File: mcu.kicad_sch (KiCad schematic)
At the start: 17 parts, among them J2 U.FL-R-SMT-1(10), U1 SF32LB525UC6, U6 GD25Q64ESIG, Y1 32.768khz, Y2 48MHz

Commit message: save progress before refactor
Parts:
- removed U6: GD25Q64ESIG, GD25Q64ESIG:SOP-8_L5.3-W5.3-P1.27-LS8.0-BL, symbol GD25Q64ESIG:GD25Q64ESIG
- removed Y1: 32.768khz, Crystal:Crystal_SMD_2520-4Pin_2.5x2.0mm, symbol Device:Crystal_Small
- added TP8: SCL, TestPoint:TestPoint_Pad_1.5x1.5mm, symbol Connector:TestPoint
- added TP9: SDA, TestPoint:TestPoint_Pad_1.5x1.5mm, symbol Connector:TestPoint
- added U6: GD25Q64CWIGR, GD25Q64CWIGR:WSON-8_L6.0-W5.0-P1.27-BL-EP, symbol GD25Q64CWIGR:GD25Q64CWIGR
- added Y3: 32.768khz, symbol Device:Crystal_Small
- AE1: LCSC Part (none) -> C89334
- C20, C22, C23, L2, L3: now not fitted; now left out of the parts list
- C21: LCSC Part (none) -> C1548
- C24: LCSC Part (none) -> C1525
- J2: LCSC Part (none) -> C88374; now not fitted
- R10, R9: LCSC Part (none) -> C25744
- TP1, TP2: now left out of the parts list
- U1: LCSC Part (none) -> C47355842
- Y2: LCSC Part (none) -> C2932991
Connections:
- net +3V3: now also U6.8 (VCC)
- net FLASH_CLK: now also U6.6 (SCLK)
- net FLASH_CS: now also U6.1 (~{CS})
- net FLASH_DIO0: now also U6.5 (SI(IO0))
- net FLASH_DIO1: now also U6.2 (SO(IO1))
- net FLASH_DIO2: now also U6.3 (WP#(IO2))
- net FLASH_DIO3: now also U6.7 (HOLD#(IO3))
- net GND: now also U6.4 (VSS), U6.9 (EP)
- net SCL: now also TP8.1
- net SDA: now also TP9.1
- net at U1.11 (PA22): now also Y3.2
- net at U1.10 (PA23): now also Y3.1
- net HAPTIC_PWM: now reaches U1.25 (PA20)
- net OLED_EN: now reaches U1.49 (PA2)
- net LED_CLK: now reaches U1.5 (PA28)
- net LED_EN: now reaches U1.6 (PA27)
- net LED_DAT: now reaches U1.9 (PA24)
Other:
- moved on the sheet: C24

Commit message: progress dump
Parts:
- added R45, R46: 4.7k, Resistor_SMD:R_0402_1005Metric, symbol Device:R_Small
- added TP10: SCL, symbol Connector:TestPoint
- added TP11: TestPoint, symbol Connector:TestPoint
- R10, R9: value 10k -> 4.7k
- TP8: value SCL -> SCL_G1
- TP9: value SDA -> SDA_G1
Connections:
- net +3V3: now also R45.2, R46.2; no longer R10.2, R9.2
- net SCL: now also R46.1, TP10.1; no longer R10.1, TP8.1
- net SDA: now also R45.1, TP11.1; no longer R9.1, TP9.1
- net SDA_G1: now reaches U1.1 (PA32)
- net SDA_G1: now also R9.1, TP9.1
- net TOUCH_RST: now reaches U1.56 (PA44)
- net TOUCH_INT: now reaches U1.57 (PA43)
- net SCL_G1: now reaches U1.67 (PA33)
- net SCL_G1: now also R10.1, TP8.1
- net LED_CLK: no longer names the net of U1.5 (PA28)
- new net +3V3_G1: R10.2, R9.2
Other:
- moved on the sheet: C24, R10, R9, TP8, TP9, U6

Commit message: finish up everything but nfc
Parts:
- removed U6: GD25Q64CWIGR, GD25Q64CWIGR:WSON-8_L6.0-W5.0-P1.27-BL-EP, symbol GD25Q64CWIGR:GD25Q64CWIGR
- added R47: 100k, Resistor_SMD:R_0402_1005Metric, symbol Device:R_Small
- added R48: 47k, Resistor_SMD:R_0402_1005Metric, symbol Device:R_Small
- added R49: 7.5k, Resistor_SMD:R_0603_1608Metric, symbol Device:R_Small
- added TP12: UART2_TX, TestPoint:TestPoint_Pad_D1.0mm, symbol Connector:TestPoint
- added TP13: UART2_RX, TestPoint:TestPoint_Pad_D1.0mm, symbol Connector:TestPoint
- added U12: MKDV1GCL-ABA, MKDV1GCL-ABA:LGA-8_L6.0-W8.0-P1.27-TL, symbol MKDV1GCL-ABA:MKDV1GCL-ABA
- R10, R45, R46, R9: LCSC Part C25744 -> C25900
- TP10: footprint (none) -> TestPoint:TestPoint_Pad_D1.0mm; now left out of the parts list
- TP11: value TestPoint -> SDA; footprint (none) -> TestPoint:TestPoint_Pad_D1.0mm; now left out of the parts list
- TP8: value SCL_G1 -> SCL_G2; footprint TestPoint:TestPoint_Pad_1.5x1.5mm -> TestPoint:TestPoint_Pad_D1.0mm
- TP9: value SDA_G1 -> SDA_G2; footprint TestPoint:TestPoint_Pad_1.5x1.5mm -> TestPoint:TestPoint_Pad_D1.0mm
- Y3: footprint (none) -> Crystal:Crystal_SMD_2012-2Pin_2.0x1.2mm; LCSC Part (none) -> C99009
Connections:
- net +3V3: no longer C24.1
- net +3V3_G1: now also C24.1, R49.1, U12.8 (VDD); no longer R10.2, R9.2
- net GND: now also U12.4 (GND)
- net HAPTIC_PWM: now also U1.6 (PA27); no longer U1.25 (PA20)
- net LED_DAT: now also U1.63 (PA37); no longer U1.9 (PA24)
- net LED_EN: now also U1.62 (PA38); no longer U1.6 (PA27)
- net TOUCH_INT: now also R47.1
- net TOUCH_RST: now also R48.1
- net UART2_RX: now reaches U1.35 (PA10)
- net UART2_RX: now also TP13.1
- net UART2_TX: now reaches U1.42 (PA9)
- net UART2_TX: now also TP12.1
- net ACC_INT: now reaches U1.61 (PA39)
- net RF_WAKE: now reaches U1.8 (PA25)
- net FLASH_CLK renamed SD_DAT0
- net SD_DAT0: now also U12.6 (DAT0)
- net FLASH_CS renamed SD_DAT2
- net SD_DAT2: now also U12.1 (DAT2)
- net FLASH_DIO0 renamed SD_CMD
- net SD_CMD: now also U12.5 (CMD)
- net FLASH_DIO1 renamed SD_DAT3
- net SD_DAT3: now also R49.2, U12.2 (DAT3)
- net FLASH_DIO2 renamed SD_CLK
- net SD_CLK: now also U12.3 (CLK)
- net FLASH_DIO3 renamed SD_DAT1
- net SD_DAT1: now also U12.7 (DAT1)
- net SCL_G1 renamed SCL_G2
- net SDA_G1 renamed SDA_G2
- new net +3V3_G2: R10.2, R47.2, R48.2, R9.2
- new net FUEL_GPOUT: U1.25 (PA20)
- new net RF_DAT: U1.9 (PA24)
- no-connect marks 5 -> 15
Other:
- note added: "Pull up to configure boot from SD Card"
- moved on the sheet: C24, R45, R46, TP10, TP11

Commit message: progress
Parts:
- removed R10, R9: 4.7k, Resistor_SMD:R_0402_1005Metric, symbol Device:R_Small
- removed R48: 47k, Resistor_SMD:R_0402_1005Metric, symbol Device:R_Small
- R45, R46: footprint Resistor_SMD:R_0402_1005Metric -> (none); LCSC Part C25900 -> (none)
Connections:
- net +3V3: now also R45.1, R46.1; no longer R45.2, R46.2
- net ACC_INT: now also U1.57 (PA43); no longer U1.61 (PA39)
- net HAPTIC_PWM: now also U1.4 (PA29); no longer U1.6 (PA27)
- net LED_DAT: now also U1.9 (PA24); no longer U1.63 (PA37)
- net LED_EN: now also U1.5 (PA28); no longer U1.62 (PA38)
- net RF_DAT: now also U1.8 (PA25); no longer U1.9 (PA24)
- net RF_WAKE: now also U1.7 (PA26); no longer U1.8 (PA25)
- net SCL: now also R46.2, U1.58 (PA42); no longer R46.1, U1.59 (PA41)
- net SCL_G2: no longer U1.67 (PA33)
- net SDA: now also R45.2, U1.59 (PA41); no longer R45.1, U1.60 (PA40)
- net SDA_G2: no longer U1.1 (PA32)
- net TOUCH_INT: now also U1.6 (PA27); no longer U1.57 (PA43)
- net SCL_T2: now reaches U1.2 (PA31)
- net SDA_T2: now reaches U1.3 (PA30)
- net TOUCH_RST renamed NFC_INT
- new net NFC_CLK: U1.61 (PA39)
- new net NFC_CS: U1.60 (PA40)
- new net NFC_DI: U1.62 (PA38)
- new net NFC_DO: U1.63 (PA37)
- new net SCL_T1: U1.67 (PA33)
- new net SDA_T1: U1.1 (PA32)
- no-connect marks 15 -> 9
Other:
- moved on the sheet: C24, R47, TP10, TP11, TP8, TP9, U12

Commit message: push changes before removing fuel gauge
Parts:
- R45, R46: footprint (none) -> Resistor_SMD:R_0402_1005Metric; LCSC Part (none) -> C25900
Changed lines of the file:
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@@
 			)
 		)
-		(property "Footprint" ""
+		(property "Footprint" "Resistor_SMD:R_0402_1005Metric"
 			(at 166.37 101.6 0)
 			(effects
@@
 		)
 		(property "VERIFIER" ""
+			(at 166.37 101.6 0)
+			(effects
+				(font
+					(size 1.27 1.27)
+				)
+				(hide yes)
+			)
+		)
+		(property "LCSC Part" "C25900"
 			(at 166.37 101.6 0)
 			(effects
@@
 			)
 		)
-		(property "Footprint" ""
+		(property "Footprint" "Resistor_SMD:R_0402_1005Metric"
 			(at 153.67 101.6 0)
 			(effects
@@
 			(at 153.67 101.6 0)
 			(effects
+				(font
+					(size 1.27 1.27)
+				)
+				(hide yes)
+			)
+		)
+		(property "LCSC Part" "C25900"
+			(at 153.67 101.6 0)
+			(effects

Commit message: hopefully final schematic before splitting out
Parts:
- renumbered C22 to C1, C21 to C2, C23 to C3, C20 to C4, C24 to C5, J2 to J1, L3 to L1, R49 to R1, R45 to R2, R47 to R3, R46 to R4, TP12 to TP1, TP13 to TP2, TP1 to TP3, TP2 to TP4, TP11 to TP5, TP10 to TP6, TP8 to TP7, TP9 to TP8, U12 to U2, Y2 to Y1, Y3 to Y2

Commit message: final review, fixes, cleanup
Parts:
- added TP16: SCL_T1, TestPoint:TestPoint_Pad_D1.0mm, symbol Connector:TestPoint
- added TP17: SDA_T1, TestPoint:TestPoint_Pad_D1.0mm, symbol Connector:TestPoint
- C4: value NF -> 1pF; LCSC Part (none) -> C37117; now fitted; now in the parts list
- J1: now fitted
- L1: value NF -> 2.7nH; LCSC Part (none) -> C412027; now fitted; now in the parts list
- L2: value NF -> 3.9nH; LCSC Part (none) -> C13818; now fitted; now in the parts list
- TP7: value SCL_G2 -> SCL_T1
- TP8: value SDA_G2 -> SDA_T1
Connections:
- net SCL_G2 is gone; now on net SCL_T1: TP7.1
- net SDA_G2 is gone; now on net SDA_T1: TP8.1
- net +3V3: no longer U1.38 (AVDD33_AUD)
- net +3V3_G1: now also U1.38 (AVDD33_AUD)
- net HAPTIC_PWM: now also U1.44 (PA7); no longer U1.4 (PA29)
- net SCL_T2: now also TP16.1
- net SDA_T2: now also TP17.1
- net HAPTIC_EN: now reaches U1.43 (PA8)
- net FUEL_GPOUT: no longer names the net of U1.25 (PA20)
- net USB_DM renamed USB_DN
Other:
- note added: "NOTE: eval board values, must be properly tuned!"
- note added: "Remove C2 & C3 for VNA"
- note removed: "Remove C21 & C23 for VNA"

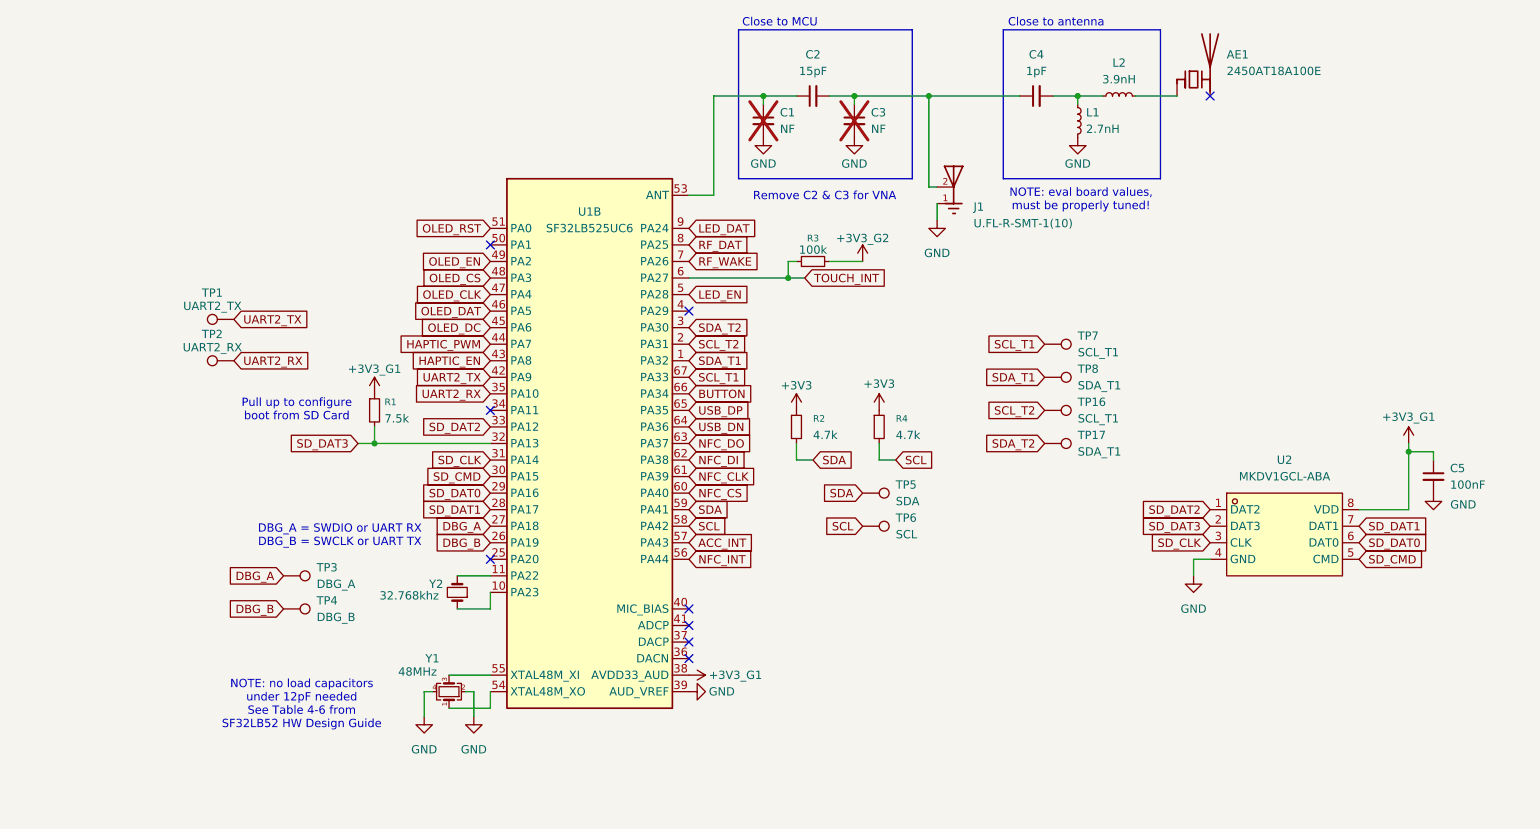
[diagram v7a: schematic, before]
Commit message: prepare schematic for devboard
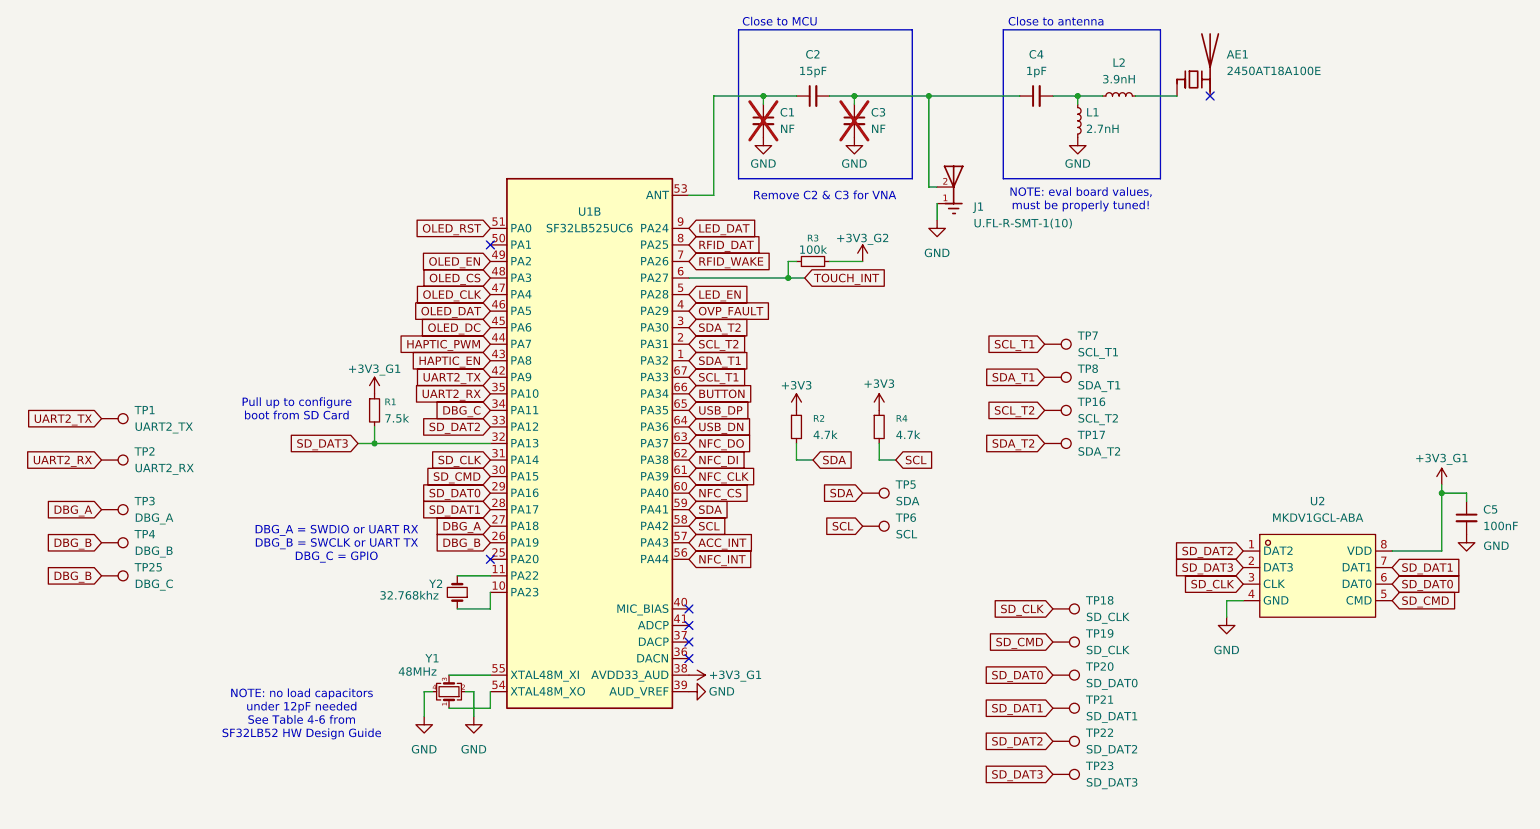
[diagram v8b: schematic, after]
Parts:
- added TP18, TP19: SD_CLK, TestPoint:TestPoint_Pad_D1.0mm, symbol Connector:TestPoint
- added TP20: SD_DAT0, TestPoint:TestPoint_Pad_D1.0mm, symbol Connector:TestPoint
- added TP21: SD_DAT1, TestPoint:TestPoint_Pad_D1.0mm, symbol Connector:TestPoint
- added TP22: SD_DAT2, TestPoint:TestPoint_Pad_D1.0mm, symbol Connector:TestPoint
- added TP23: SD_DAT3, TestPoint:TestPoint_Pad_D1.0mm, symbol Connector:TestPoint
- added TP25: DBG_C, TestPoint:TestPoint_Pad_D1.0mm, symbol Connector:TestPoint
- TP16: value SCL_T1 -> SCL_T2
- TP17: value SDA_T1 -> SDA_T2
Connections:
- net DBG_B: now also TP25.1
- net SD_CLK: now also TP18.1
- net SD_CMD: now also TP19.1
- net SD_DAT0: now also TP20.1
- net SD_DAT1: now also TP21.1
- net SD_DAT2: now also TP22.1
- net SD_DAT3: now also TP23.1
- net DBG_C: now reaches U1.34 (PA11)
- net OVP_FAULT: now reaches U1.4 (PA29)
- net RF_DAT renamed RFID_DAT
- net RF_WAKE renamed RFID_WAKE
- no-connect marks 9 -> 7
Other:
- note added: "DBG_A = SWDIO or UART RX DBG_B = SWCLK or UART TX DBG_C = GPIO"
- note removed: "DBG_A = SWDIO or UART RX DBG_B = SWCLK or UART TX"
- moved on the sheet: C5, TP3, TP4, U2
